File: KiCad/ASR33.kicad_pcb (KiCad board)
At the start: 2 copper layers, 45 x 38 mm, 42 parts, among them J1 USB-C, J2 DC, J3 Power, J4 RUN, J5 Tx, J6 Rx, Q1 NX7002AK, SW1 SW_Push, U1 ESP32-WROOM-32, U2 FT231XQ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

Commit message: More tinkering
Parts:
- D4: value D -> Schottky
- moved Logo1 24.2 mm to (123.3, 86.0)
- moved C1 2.19 mm to (131.3, 90.8), turned to 180 degrees
- moved R9 1.81 mm to (124.5, 97.2)
- moved R8 1.09 mm to (121.7, 97.2), turned to 0 degrees
- moved R10 0.41 mm to (131.2, 106.0)
- moved R5 0.40 mm to (129.1, 106.8)
- moved U7 0.30 mm to (155.0, 86.3)
- moved R4 0.30 mm to (129.1, 102.0)
- moved C4 0.29 mm to (127.5, 110.8)
- moved Q1 0.25 mm to (135.8, 109.4)
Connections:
- U1 pad 36: PWR -> MTR
- U1 pad 37: MTR -> PWR
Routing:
- net DC: track 51.6 -> 71.8 mm, vias 2 -> 1
- net PWR: track 15.8 -> 35.7 mm
- net Net-(C3-Pad1): track 18.0 -> 22.5 mm
- net GND: track 20.0 -> 16.9 mm, vias 6 -> 1
- net Net-(C2-Pad1): track 24.8 -> 21.7 mm, vias 0 -> 2
- net +3V3: track 89.5 -> 91.1 mm
- net Net-(C6-Pad2): track 18.4 -> 17.2 mm
- net Net-(J5-Pad3): track 9.68 -> 8.70 mm
- net Net-(C1-Pad1): track 16.3 -> 15.3 mm
- net MTR: track 18.0 -> 18.8 mm
- net VBUS: track 32.8 -> 32.1 mm
- net Net-(C5-Pad1): track 14.3 -> 13.6 mm

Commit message: Tinker
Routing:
- net Net-(C6-Pad2): track 17.2 -> 18.6 mm
- net Net-(C6-Pad1): track 13.1 -> 13.9 mm
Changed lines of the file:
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@@
       (primitives
     (gr_arc (start 2.89 -3.045) (mid 0 -0.155) (end -2.89 -3.045) (width 0.25))
-    (gr_arc (start 4.294753 -3.49127) (mid -0.020907 -1.02625) (end -4.315692 -3.527464) (width 0.25))
+    (gr_arc (start 4.294753 -3.49127) (mid -0.016568 -1.026234) (end -4.311371 -3.519937) (width 0.25))
     (gr_arc (start -3.2 -2.485) (mid -4.015 -3.3) (end -3.2 -4.115) (width 0.25))
     (gr_arc (start 3.2 -4.115) (mid 4.015 -3.3) (end 3.2 -2.485) (width 0.25))
-    (gr_arc (start -4.32 0.635) (mid 0 -1.154403) (end 4.32 0.635) (width 0.25))
+    (gr_arc (start -4.32 0.635) (mid -0.000001 -1.154403) (end 4.319999 0.634999) (width 0.25))
         (gr_poly (pts
             (xy 3.75 0.085)
@@
         (gr_circle (center 0 0.25) (end 0.5 0.25) (width 0) (fill yes))
         (gr_poly (pts
+            (xy 0.5 0.75)
+            (xy 0 0.75)
+            (xy 0 -0.75)
             (xy 0.5 -0.75)
-            (xy 0 -0.75)
-            (xy 0 0.75)
-            (xy 0.5 0.75)
           ) (width 0) (fill yes))
       ))
@@
         (gr_circle (center 0 0.25) (end 0.5 0.25) (width 0) (fill yes))
         (gr_poly (pts
+            (xy 0 0.75)
+            (xy -0.5 0.75)
+            (xy -0.5 -0.75)
             (xy 0 -0.75)
-            (xy -0.5 -0.75)
-            (xy -0.5 0.75)
-            (xy 0 0.75)
           ) (width 0) (fill yes))
       ))
@@
     (effects (font (size 1 1) (thickness 0.15)) (justify mirror))
   )
+  (gr_text "www.me.uk" (at 123.75 90) (layer "B.SilkS")
+    (effects (font (size 0.8 0.8) (thickness 0.15)) (justify mirror))
+  )
   (gr_text "20mA" (at 132.5 111.5) (layer "B.SilkS")
     (effects (font (size 1 1) (thickness 0.15)) (justify mirror))
@@
     (effects (font (size 1.5 1.5) (thickness 0.2)) (justify mirror))
   )
-  (gr_text "www.me.uk" (at 123.75 90) (layer "B.SilkS")
-    (effects (font (size 0.8 0.8) (thickness 0.15)) (justify mirror))
-  )
   (gr_text "3.3V" (at 160 111.5) (layer "B.SilkS")
     (effects (font (size 1 1) (thickness 0.15)) (justify mirror))
@@
   (gr_text "⏚" (at 122.5 117.5 270) (layer "F.SilkS")
     (effects (font (size 1 1) (thickness 0.2)))
+  )
+  (gr_text "${DATE}" (at 157.4 91.5 270) (layer "F.SilkS")
+    (effects (font (size 1 1) (thickness 0.15)))
   )
   (gr_text "RUN" (at 152.5 117.5 270) (layer "F.SilkS")
@@
   (segment (start 134.2 103) (end 132.2 103) (width 0.25) (layer "B.Cu") (net 41))
   (arc (start 132.2 103) (mid 132.129289 103.029289) (end 132.1 103.1) (width 0.25) (layer "B.Cu") (net 41))
-  (segment (start 139 108.625) (end 139 106.52) (width 0.25) (layer "F.Cu") (net 44))
+  (segment (start 138.4 108.4) (end 138.4 107.12) (width 0.25) (layer "F.Cu") (net 44))
   (segment (start 140 109.625) (end 140 113.4) (width 0.25) (layer "F.Cu") (net 44))
-  (arc (start 139 106.52) (mid 139.102513 106.272513) (end 139.35 106.17) (width 0.25) (layer "F.Cu") (net 44))
+  (segment (start 139 108.625) (end 138.625 108.625) (width 0.25) (layer "F.Cu") (net 44))
+  (arc (start 138.4 107.12) (mid 138.678249 106.448249) (end 139.35 106.17) (width 0.25) (layer "F.Cu") (net 44))
+  (arc (start 138.625 108.625) (mid 138.465901 108.559099) (end 138.4 108.4) (width 0.25) (layer "F.Cu") (net 44))
   (arc (start 139 108.625) (mid 139.707107 108.917893) (end 140 109.625) (width 0.25) (layer "F.Cu") (net 44))
   (segment (start 140 110.5) (end 140 113.4) (width 0.25) (layer "B.Cu") (net 44))
@@
   (arc (start 139.25 109.75) (mid 139.78033 109.96967) (end 140 110.5) (width 0.25) (layer "B.Cu") (net 44))
   (segment (start 135 114.75) (end 133.25 114.75) (width 0.25) (layer "F.Cu") (net 45))
-  (segment (start 136.25 110.5) (end 136.25 113.5) (width 0.25) (layer "F.Cu") (net 45))
+  (segment (start 136.25 113.203553) (end 136.25 113.5) (width 0.25) (layer "F.Cu") (net 45))
   (segment (start 132.5 113.4) (end 132.5 114) (width 0.25) (layer "F.Cu") (net 45))
+  (segment (start 135.75 110.3375) (end 135.75 111.996447) (width 0.25) (layer "F.Cu") (net 45))
   (segment (start 135.75 110.3375) (end 135.75 106.9) (width 0.25) (layer "F.Cu") (net 45))
-  (segment (start 135.75 110.3375) (end 136.0875 110.3375) (width 0.25) (layer "F.Cu") (net 45))
+  (arc (start 135.75 111.996447) (mid 135.814972 112.323087) (end 136 112.6) (width 0.25) (layer "F.Cu") (net 45))
   (arc (start 135 114.75) (mid 135.883883 114.383883) (end 136.25 113.5) (width 0.25) (layer "F.Cu") (net 45))
   (arc (start 135.75 106.9) (mid 135.96967 106.36967) (end 136.5 106.15) (width 0.25) (layer "F.Cu") (net 45))
   (arc (start 132.5 114) (mid 132.71967 114.53033) (end 133.25 114.75) (width 0.25) (layer "F.Cu") (net 45))
-  (arc (start 136.0875 110.3375) (mid 136.202405 110.385095) (end 136.25 110.5) (width 0.25) (layer "F.Cu") (net 45))
+  (arc (start 136 112.6) (mid 136.185027 112.876912) (end 136.25 113.203553) (width 0.25) (layer "F.Cu") (net 45))
+  (segment (start 138.8 114.1) (end 138.8 112.4) (width 0.25) (layer "F.Cu") (net 46))
+  (segment (start 139.5 110.5) (end 139.5 111.7) (width 0.25) (layer "F.Cu") (net 46))
+  (segment (start 138.17 103.63) (end 139.35 103.63) (width 0.25) (layer "F.Cu") (net 46))
+  (segment (start 137.9 109.7) (end 137.9 103.9) (width 0.25) (layer "F.Cu") (net 46))
   (segment (start 142.5 113.4) (end 142.5 114.4) (width 0.25) (layer "F.Cu") (net 46))
-  (segment (start 139 110.175) (end 138.675 110.175) (width 0.25) (layer "F.Cu") (net 46))
   (segment (start 142.2 114.7) (end 139.4 114.7) (width 0.25) (layer "F.Cu") (net 46))
-  (segment (start 138.8 114.1) (end 138.8 110.375) (width 0.25) (layer "F.Cu") (net 46))
-  (segment (start 139.27 103.63) (end 139.35 103.63) (width 0.25) (layer "F.Cu") (net 46))
-  (segment (start 138.025489 104.874511) (end 138.025489 109.525489) (width 0.25) (layer "F.Cu") (net 46))
-  (arc (start 138.675 110.175) (mid 138.215726 109.984763) (end 138.025489 109.525489) (width 0.25) (layer "F.Cu") (net 46))
+  (segment (start 139 110.175) (end 139.175 110.175) (width 0.25) (layer "F.Cu") (net 46))
+  (segment (start 138.375 110.175) (end 139 110.175) (width 0.25) (layer "F.Cu") (net 46))
+  (arc (start 139.2 112) (mid 138.917157 112.117157) (end 138.8 112.4) (width 0.25) (layer "F.Cu") (net 46))
+  (arc (start 139.175 110.175) (mid 139.40481 110.27019) (end 139.5 110.5) (width 0.25) (layer "F.Cu") (net 46))
+  (arc (start 137.9 103.9) (mid 137.979081 103.709081) (end 138.17 103.63) (width 0.25) (layer "F.Cu") (net 46))
+  (arc (start 137.9 109.7) (mid 138.039124 110.035876) (end 138.375 110.175) (width 0.25) (layer "F.Cu") (net 46))
   (arc (start 142.5 114.4) (mid 142.412132 114.612132) (end 142.2 114.7) (width 0.25) (layer "F.Cu") (net 46))
-  (arc (start 138.8 110.375) (mid 138.858579 110.233579) (end 139 110.175) (width 0.25) (layer "F.Cu") (net 46))
+  (arc (start 139.2 112) (mid 139.412132 111.912132) (end 139.5 111.7) (width 0.25) (layer "F.Cu") (net 46))
   (arc (start 139.4 114.7) (mid 138.975736 114.524264) (end 138.8 114.1) (width 0.25) (layer "F.Cu") (net 46))
-  (arc (start 138.025489 104.874511) (mid 138.389998 103.994509) (end 139.27 103.63) (width 0.25) (layer "F.Cu") (net 46))
   (segment (start 148.8 106) (end 148.8 103.1) (width 0.25) (layer "F.Cu") (net 51))
+  (segment (start 140.605 87.305) (end 139.995 87.305) (width 0.25) (layer "F.Cu") (net 51))
   (segment (start 138.79001 87.305) (end 139.995 87.305) (width 0.25) (layer "F.Cu") (net 51))
-  (segment (start 141.6 88.2) (end 141.6 95.3) (width 0.25) (layer "F.Cu") (net 51))
-  (segment (start 139.995 87.305) (end 140.705 87.305) (width 0.25) (layer "F.Cu") (net 51))
-  (segment (start 151.7 96.6) (end 142.9 96.6) (width 0.25) (layer "F.Cu") (net 51))
+  (segment (start 141.4 96) (end 141.4 88.1) (width 0.25) (layer "F.Cu") (net 51))
   (segment (start 148.8 109.125) (end 148.8 106) (width 0.25) (layer "F.Cu") (net 51))
+  (segment (start 151.7 96.6) (end 142 96.6) (width 0.25) (layer "F.Cu") (net 51))
   (segment (start 150.3 110.05) (end 149.725 110.05) (width 0.25) (layer "F.Cu") (net 51))
   (via (at 151.7 96.6) (size 0.8) (drill 0.4) (layers "F.Cu" "B.Cu") (net 51))
   (via (at 148.8 103.1) (size 0.8) (drill 0.4) (layers "F.Cu" "B.Cu") (net 51))
-  (arc (start 141.6 95.3) (mid 141.980761 96.219239) (end 142.9 96.6) (width 0.25) (layer "F.Cu") (net 51))
+  (arc (start 142 96.6) (mid 141.575736 96.424264) (end 141.4 96) (width 0.25) (layer "F.Cu") (net 51))
   (arc (start 136.75 88.15) (mid 137.685964 87.524609) (end 138.79001 87.305) (width 0.25) (layer "F.Cu") (net 51))
   (arc (start 149.725 110.05) (mid 149.070926 109.779074) (end 148.8 109.125) (width 0.25) (layer "F.Cu") (net 51))
-  (arc (start 140.705 87.305) (mid 141.337861 87.567139) (end 141.6 88.2) (width 0.25) (layer "F.Cu") (net 51))
+  (arc (start 141.4 88.1) (mid 141.16715 87.53785) (end 140.605 87.305) (width 0.25) (layer "F.Cu") (net 51))
   (segment (start 154.5 100.1) (end 154.5 98) (width 0.25) (layer "B.Cu") (net 51))
   (segment (start 136.75 88.15) (end 130.25 88.15) (width 0.25) (layer "B.Cu") (net 51))

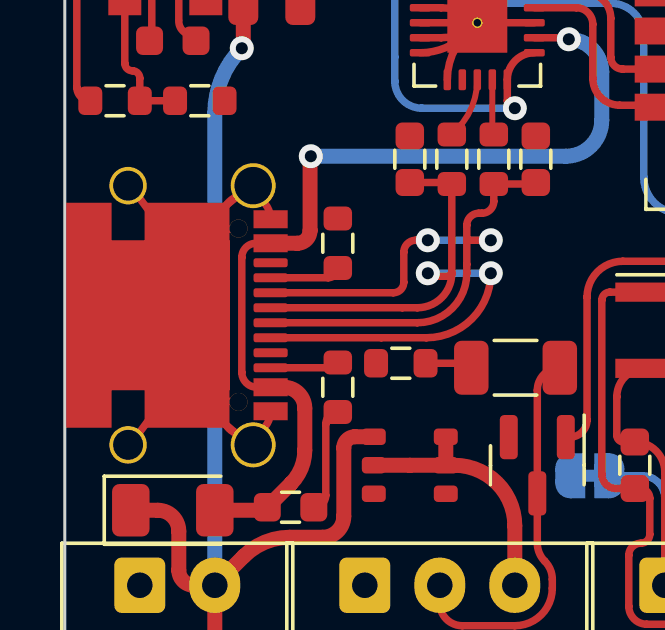
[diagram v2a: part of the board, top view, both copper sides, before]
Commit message: Fix resistor values on LED
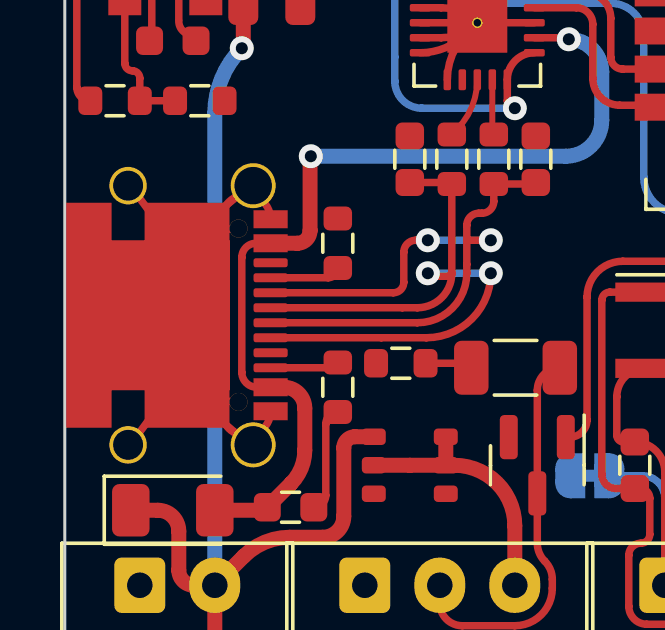
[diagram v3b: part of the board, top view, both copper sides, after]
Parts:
- R1: value 1K -> 680R
- R3: value 470R -> 220R
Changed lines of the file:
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@@
       (primitives
     (gr_arc (start 2.89 -3.045) (mid 0 -0.155) (end -2.89 -3.045) (width 0.25))
-    (gr_arc (start 4.294753 -3.49127) (mid -0.016568 -1.026234) (end -4.311371 -3.519937) (width 0.25))
+    (gr_arc (start 4.294753 -3.49127) (mid -0.012228 -1.026222) (end -4.307036 -3.512417) (width 0.25))
     (gr_arc (start -3.2 -2.485) (mid -4.015 -3.3) (end -3.2 -4.115) (width 0.25))
     (gr_arc (start 3.2 -4.115) (mid 4.015 -3.3) (end 3.2 -2.485) (width 0.25))
@@
       (effects (font (size 0.5 0.5) (thickness 0.08)))
     )
-    (fp_text value "470R" (at 0 0 90) (layer "F.Fab")
+    (fp_text value "220R" (at 0 0 90) (layer "F.Fab")
       (effects (font (size 0.4 0.4) (thickness 0.08)))
     )
@@
       (effects (font (size 0.5 0.5) (thickness 0.08)))
     )
-    (fp_text value "1K" (at 0 0 90) (layer "F.Fab")
-      (effects (font (size 0.4 0.4) (thickness 0.08)))
-    )
+    (fp_text value "680R" (at 0 0 90) (layer "F.Fab")
+      (effects (font (size 0.4 0.4) (thickness 0.08)))
+    )
